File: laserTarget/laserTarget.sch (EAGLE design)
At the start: 13 parts, among them Q1 MOSFET-NCHANNELBSS123LT1G, Q2 2n3904, U1 red

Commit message: Stupid. Sensor output not connected (was connected to 5V instead...)
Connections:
- net 5V: no longer U$1.+IN
- net N$1: now also U$1.+IN
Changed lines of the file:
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@@
 <pinref part="U1" gate="G$1" pin="A"/>
 <wire x1="17.78" y1="30.48" x2="17.78" y2="27.94" width="0.1524" layer="91"/>
+<pinref part="U$1" gate="G$1" pin="+IN"/>
+<wire x1="40.64" y1="38.1" x2="30.48" y2="38.1" width="0.1524" layer="91"/>
+<wire x1="30.48" y1="38.1" x2="30.48" y2="27.94" width="0.1524" layer="91"/>
+<wire x1="30.48" y1="27.94" x2="17.78" y2="27.94" width="0.1524" layer="91"/>
+<junction x="17.78" y="27.94"/>
 </segment>
 </net>
@@
 <pinref part="SUPPLY2" gate="G$1" pin="5V"/>
 <pinref part="U1" gate="G$1" pin="C"/>
-<wire x1="17.78" y1="38.1" x2="17.78" y2="40.64" width="0.1524" layer="91"/>
-<wire x1="17.78" y1="38.1" x2="17.78" y2="35.56" width="0.1524" layer="91"/>
-<wire x1="17.78" y1="38.1" x2="40.64" y2="38.1" width="0.1524" layer="91"/>
-<junction x="17.78" y="38.1"/>
-<pinref part="U$1" gate="G$1" pin="+IN"/>
+<wire x1="17.78" y1="40.64" x2="17.78" y2="35.56" width="0.1524" layer="91"/>
 </segment>
 <segment>

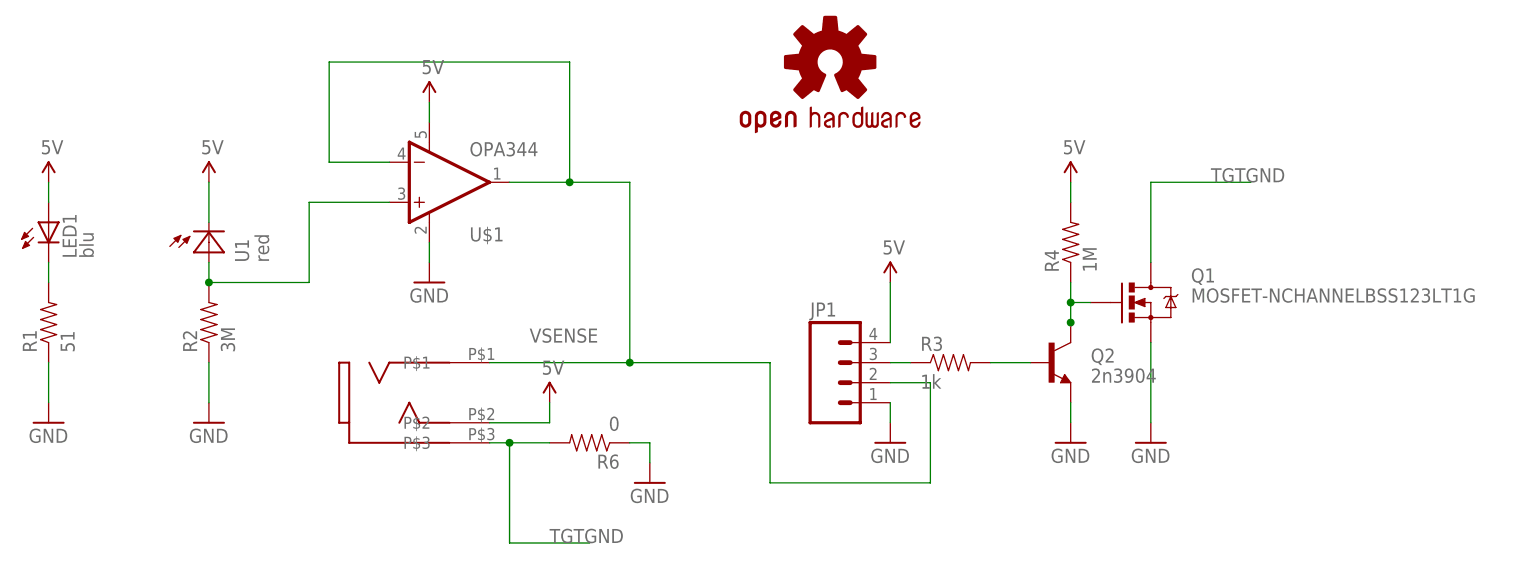
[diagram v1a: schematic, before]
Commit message: Removed test stuff from target
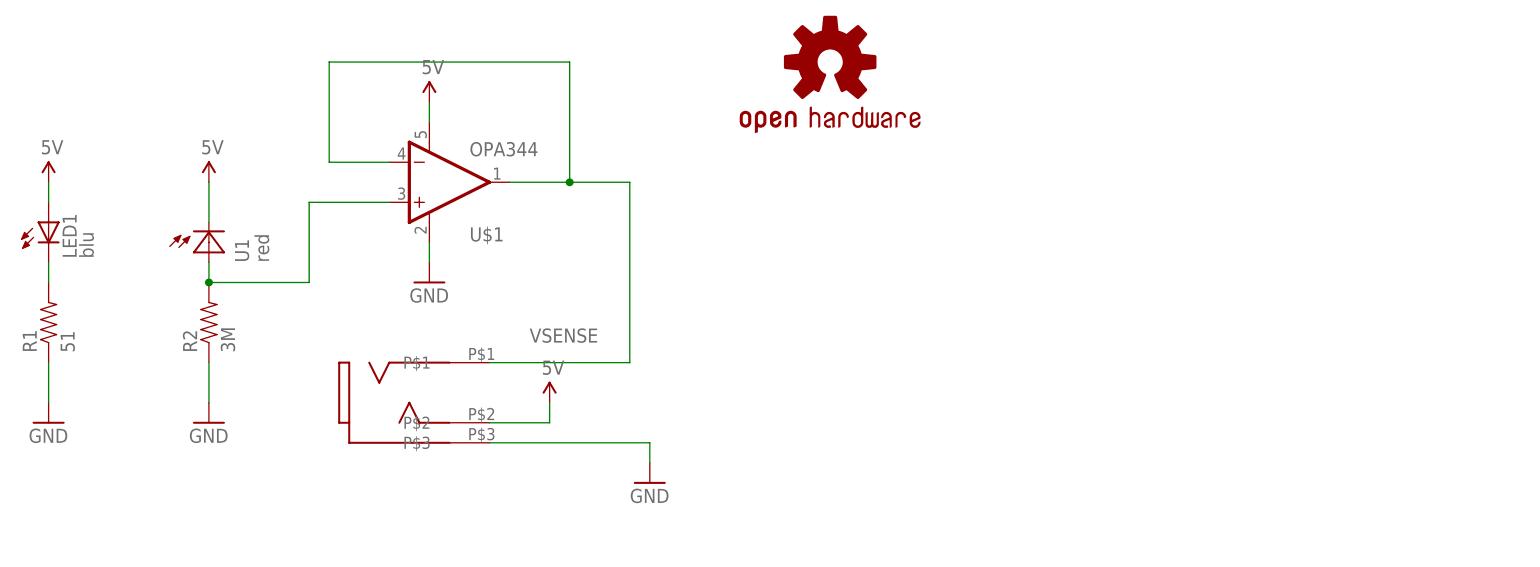
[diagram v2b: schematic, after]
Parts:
- removed JP1: (no value), SparkFun-Connectors:M04PTH
- removed Q1: MOSFET-NCHANNELBSS123LT1G, SparkFun-DiscreteSemi:MOSFET-NCHANNELBSS123LT1G
- removed Q2: 2n3904, SparkFun-DiscreteSemi:TRANSISTOR_NPNSOT23-3
- removed R3: 1k, SparkFun-Resistors:RESISTOR0805-RES
- removed R4: 1M, SparkFun-Resistors:RESISTOR0805-RES
- removed R6: 0, SparkFun-Resistors:RESISTOR0805-RES
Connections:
- removed net N$3: JP1.3, R3.1
- removed net N$4: Q2.B, R3.2
- removed net N3: Q1.G, Q2.C, R4.1
- removed net TGTGND: Q1.D, R6.2, U$2.P$3
- net 5V: no longer JP1.4, R4.2
- net GND: now also U$2.P$3; no longer JP1.1, Q1.S, Q2.E, R6.1
- net VSENSE: no longer JP1.2
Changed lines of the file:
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@@
 <part name="GND4" library="SparkFun-Aesthetics" deviceset="GND" device=""/>
 <part name="SUPPLY4" library="SparkFun-Aesthetics" deviceset="5V" device=""/>
-<part name="R3" library="SparkFun-Resistors" deviceset="RESISTOR" device="0805-RES" value="1k"/>
-<part name="R4" library="SparkFun-Resistors" deviceset="RESISTOR" device="0805-RES" value="1M"/>
-<part name="Q1" library="SparkFun-DiscreteSemi" deviceset="MOSFET-NCHANNEL" device="BSS123LT1G"/>
-<part name="Q2" library="SparkFun-DiscreteSemi" deviceset="TRANSISTOR_NPN" device="SOT23-3" value="2n3904"/>
-<part name="SUPPLY5" library="SparkFun-Aesthetics" deviceset="5V" device=""/>
-<part name="GND5" library="SparkFun-Aesthetics" deviceset="GND" device=""/>
-<part name="GND6" library="SparkFun-Aesthetics" deviceset="GND" device=""/>
-<part name="R6" library="SparkFun-Resistors" deviceset="RESISTOR" device="0805-RES" value="0"/>
-<part name="SUPPLY6" library="SparkFun-Aesthetics" deviceset="5V" device=""/>
-<part name="GND7" library="SparkFun-Aesthetics" deviceset="GND" device=""/>
-<part name="JP1" library="SparkFun-Connectors" deviceset="M04" device="PTH"/>
 <part name="LOGO1" library="SparkFun-Aesthetics" deviceset="OSHW-LOGO" device="S"/>
 </parts>
@@
 <instance part="GND4" gate="1" x="73.66" y="2.54"/>
 <instance part="SUPPLY4" gate="G$1" x="60.96" y="12.7"/>
-<instance part="R3" gate="G$1" x="111.76" y="17.78"/>
-<instance part="R4" gate="G$1" x="127" y="33.02" rot="R90"/>
-<instance part="Q1" gate="G$1" x="137.16" y="25.4"/>
-<instance part="Q2" gate="G$1" x="124.46" y="17.78"/>
-<instance part="SUPPLY5" gate="G$1" x="127" y="40.64"/>
-<instance part="GND5" gate="1" x="127" y="7.62"/>
-<instance part="GND6" gate="1" x="137.16" y="7.62"/>
-<instance part="R6" gate="G$1" x="66.04" y="7.62" rot="R180"/>
-<instance part="SUPPLY6" gate="G$1" x="104.14" y="27.94"/>
-<instance part="GND7" gate="1" x="104.14" y="7.62"/>
-<instance part="JP1" gate="G$1" x="99.06" y="15.24"/>
 <instance part="LOGO1" gate="G$1" x="96.52" y="55.88"/>
 </instances>
@@
 </segment>
 <segment>
-<pinref part="Q2" gate="G$1" pin="E"/>
-<pinref part="GND5" gate="1" pin="GND"/>
-<wire x1="127" y1="10.16" x2="127" y2="12.7" width="0.1524" layer="91"/>
-</segment>
-<segment>
-<pinref part="Q1" gate="G$1" pin="S"/>
-<pinref part="GND6" gate="1" pin="GND"/>
-<wire x1="137.16" y1="10.16" x2="137.16" y2="20.32" width="0.1524" layer="91"/>
-</segment>
-<segment>
-<pinref part="R6" gate="G$1" pin="1"/>
 <pinref part="GND4" gate="1" pin="GND"/>
-<wire x1="71.12" y1="7.62" x2="73.66" y2="7.62" width="0.1524" layer="91"/>
 <wire x1="73.66" y1="7.62" x2="73.66" y2="5.08" width="0.1524" layer="91"/>
-</segment>
-<segment>
-<pinref part="JP1" gate="G$1" pin="1"/>
-<pinref part="GND7" gate="1" pin="GND"/>
-<wire x1="104.14" y1="10.16" x2="104.14" y2="12.7" width="0.1524" layer="91"/>
+<pinref part="U$2" gate="G$1" pin="P$3"/>
+<wire x1="53.34" y1="7.62" x2="73.66" y2="7.62" width="0.1524" layer="91"/>
 </segment>
 </net>
@@
 <wire x1="60.96" y1="10.16" x2="53.34" y2="10.16" width="0.1524" layer="91"/>
 </segment>
-<segment>
-<pinref part="R4" gate="G$1" pin="2"/>
-<pinref part="SUPPLY5" gate="G$1" pin="5V"/>
-<wire x1="127" y1="40.64" x2="127" y2="38.1" width="0.1524" layer="91"/>
-</segment>
-<segment>
-<pinref part="JP1" gate="G$1" pin="4"/>
-<pinref part="SUPPLY6" gate="G$1" pin="5V"/>
-<wire x1="104.14" y1="27.94" x2="104.14" y2="20.32" width="0.1524" layer="91"/>
-</segment>
 </net>
 <net name="N$2" class="0">
@@
 <label x="58.42" y="20.32" size="1.778" layer="95"/>
 <junction x="63.5" y="40.64"/>
-<wire x1="71.12" y1="17.78" x2="88.9" y2="17.78" width="0.1524" layer="91"/>
-<wire x1="88.9" y1="17.78" x2="88.9" y2="2.54" width="0.1524" layer="91"/>
-<wire x1="88.9" y1="2.54" x2="109.22" y2="2.54" width="0.1524" layer="91"/>
-<wire x1="109.22" y1="2.54" x2="109.22" y2="15.24" width="0.1524" layer="91"/>
-<pinref part="JP1" gate="G$1" pin="2"/>
-<wire x1="109.22" y1="15.24" x2="104.14" y2="15.24" width="0.1524" layer="91"/>
-<junction x="71.12" y="17.78"/>
 </segment>
 </net>
-<net name="N3" class="0">
-<segment>
-<pinref part="Q2" gate="G$1" pin="C"/>
-<pinref part="Q2" gate="G$1" pin="C"/>
-<pinref part="R4" gate="G$1" pin="1"/>
-<wire x1="127" y1="22.86" x2="127" y2="25.4" width="0.1524" layer="91"/>
-<wire x1="127" y1="27.94" x2="127" y2="25.4" width="0.1524" layer="91"/>
-<pinref part="Q1" gate="G$1" pin="G"/>
-<wire x1="127" y1="25.4" x2="129.54" y2="25.4" width="0.1524" layer="91"/>
-<junction x="127" y="25.4"/>
-<junction x="127" y="22.86"/>
-</segment>
-</net>
-<net name="N$4" class="0">
-<segment>
-<pinref part="R3" gate="G$1" pin="2"/>
-<pinref part="Q2" gate="G$1" pin="B"/>
-<wire x1="121.92" y1="17.78" x2="116.84" y2="17.78" width="0.1524" layer="91"/>
-</segment>
-</net>
-<net name="TGTGND" class="0">
-<segment>
-<pinref part="Q1" gate="G$1" pin="D"/>
-<wire x1="137.16" y1="30.48" x2="137.16" y2="40.64" width="0.1524" layer="91"/>
-<wire x1="137.16" y1="40.64" x2="149.86" y2="40.64" width="0.1524" layer="91"/>
-<label x="144.78" y="40.64" size="1.778" layer="95"/>
-</segment>
-<segment>
-<pinref part="U$2" gate="G$1" pin="P$3"/>
-<pinref part="R6" gate="G$1" pin="2"/>
-<wire x1="60.96" y1="7.62" x2="55.88" y2="7.62" width="0.1524" layer="91"/>
-<wire x1="55.88" y1="7.62" x2="53.34" y2="7.62" width="0.1524" layer="91"/>
-<wire x1="55.88" y1="7.62" x2="55.88" y2="-5.08" width="0.1524" layer="91"/>
-<wire x1="55.88" y1="-5.08" x2="66.04" y2="-5.08" width="0.1524" layer="91"/>
-<label x="60.96" y="-5.08" size="1.778" layer="95"/>
-<junction x="55.88" y="7.62"/>
-</segment>
-</net>
-<net name="N$3" class="0">
-<segment>
-<pinref part="R3" gate="G$1" pin="1"/>
-<pinref part="JP1" gate="G$1" pin="3"/>
-<wire x1="104.14" y1="17.78" x2="106.68" y2="17.78" width="0.1524" layer="91"/>
-</segment>
-</net>
